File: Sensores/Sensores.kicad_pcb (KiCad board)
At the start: 2 copper layers, 36.6 x 32 mm, 18 parts, among them IC1 LF353, J1 GFCI, J2 NTC 3950, J3 PZEM 00T 100A, J4 ALIMENTACION

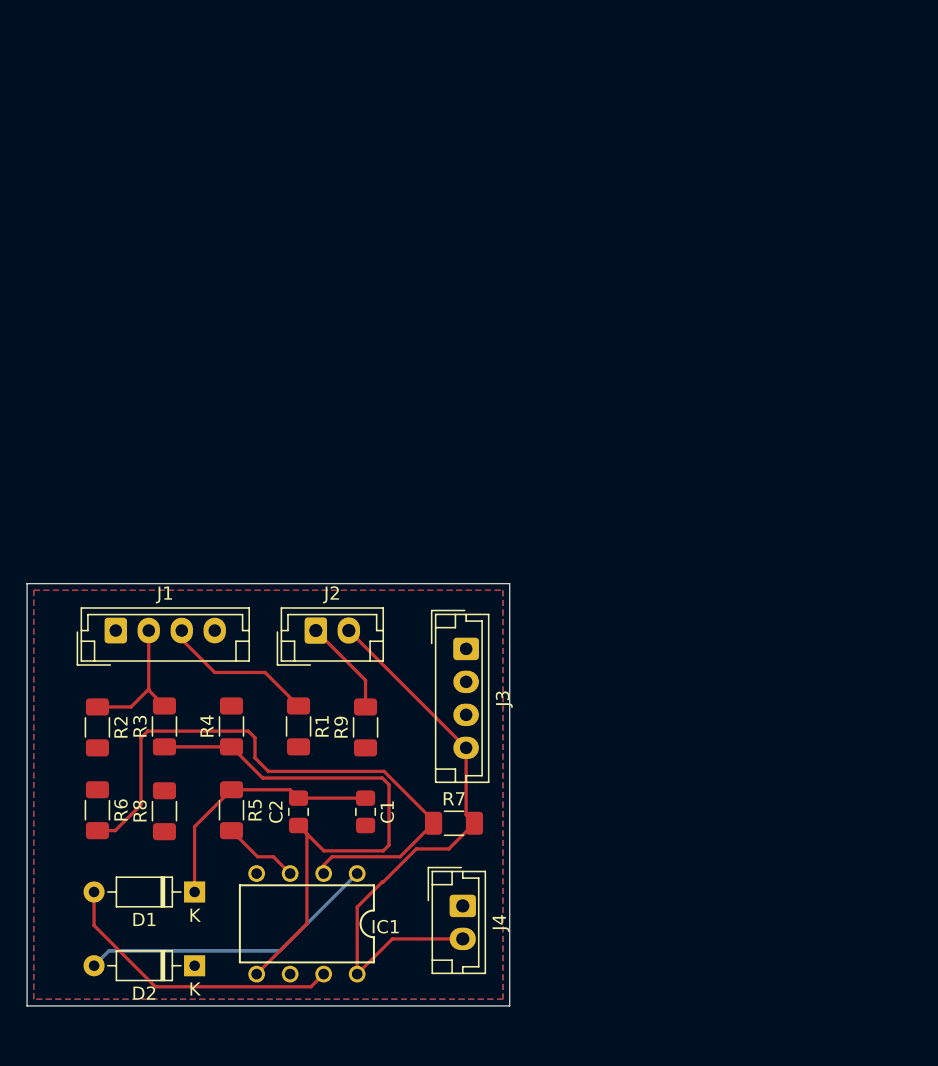
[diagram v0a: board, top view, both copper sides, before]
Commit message: footprint del pzem 004t
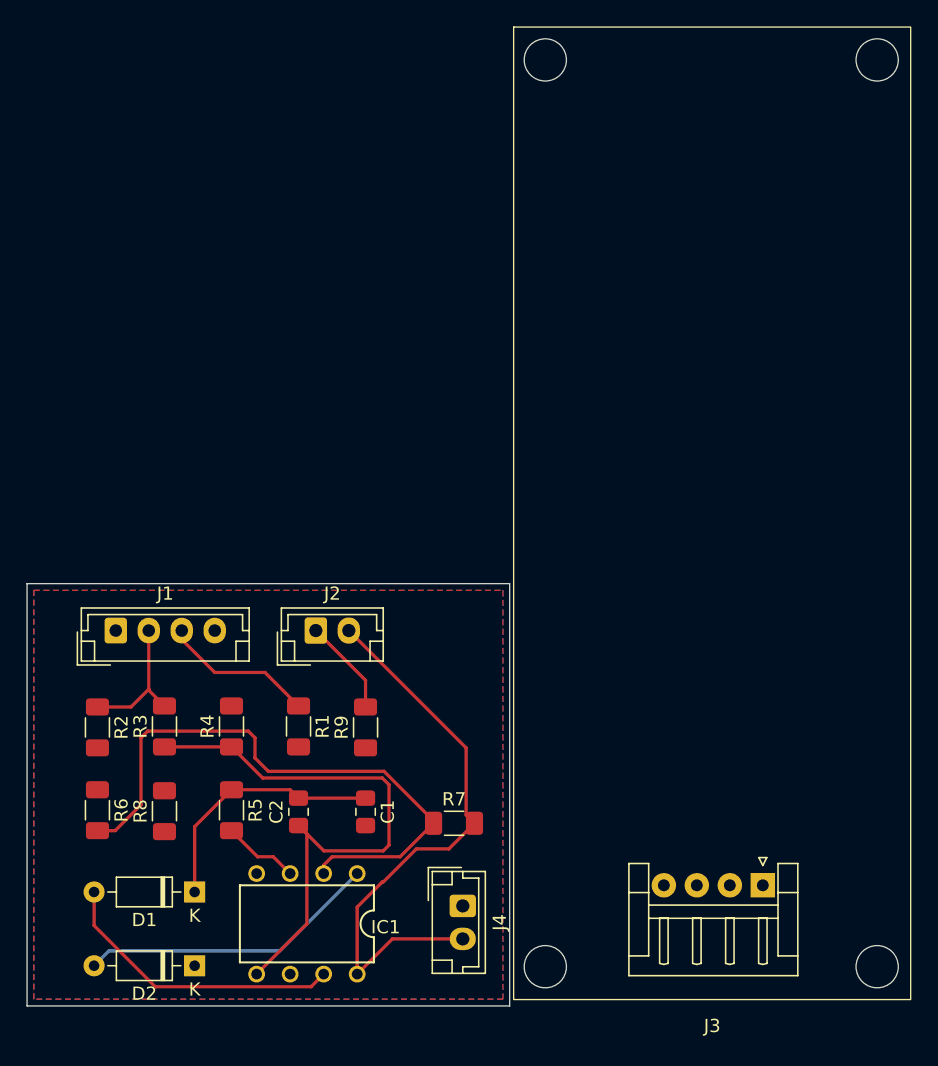
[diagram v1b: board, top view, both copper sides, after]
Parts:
- J3: value PZEM 00T 100A -> PZEM 004T 100A; footprint Connector_JST:JST_EH_B4B-EH-A_1x04_P2.50mm_Vertical -> PZEM:PZEM
- moved J3 34.5 mm to (75.8, 53.3), turned to 0 degrees
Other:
- board size 36.6 x 32 mm -> 28.3 x 71.9 mm
